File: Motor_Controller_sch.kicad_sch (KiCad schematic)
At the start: 59 parts, among them J1 1988804, J10 1988862, J11 Barrel_Jack_Switch, J12 +5V, J13 1988862, J14 1988817, J2 GND, J3 RX, J4 TX, J5 RESET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

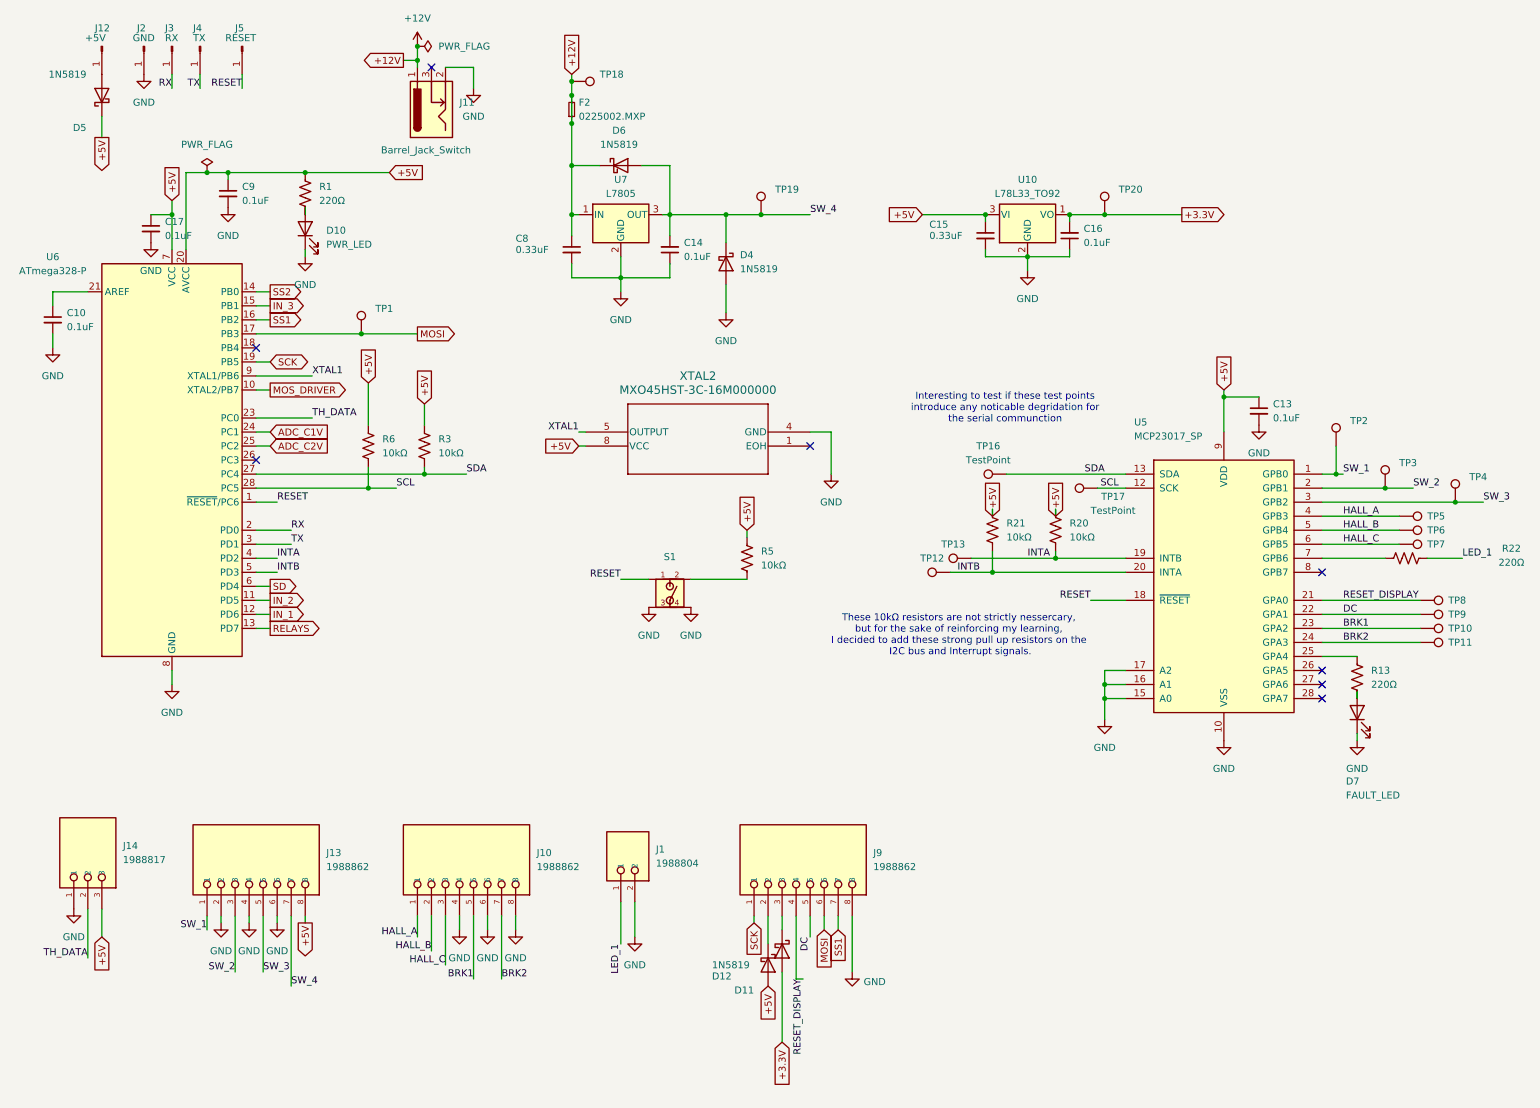
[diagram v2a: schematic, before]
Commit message: Reviewed gate resistors and removed MOSFET driver resistor
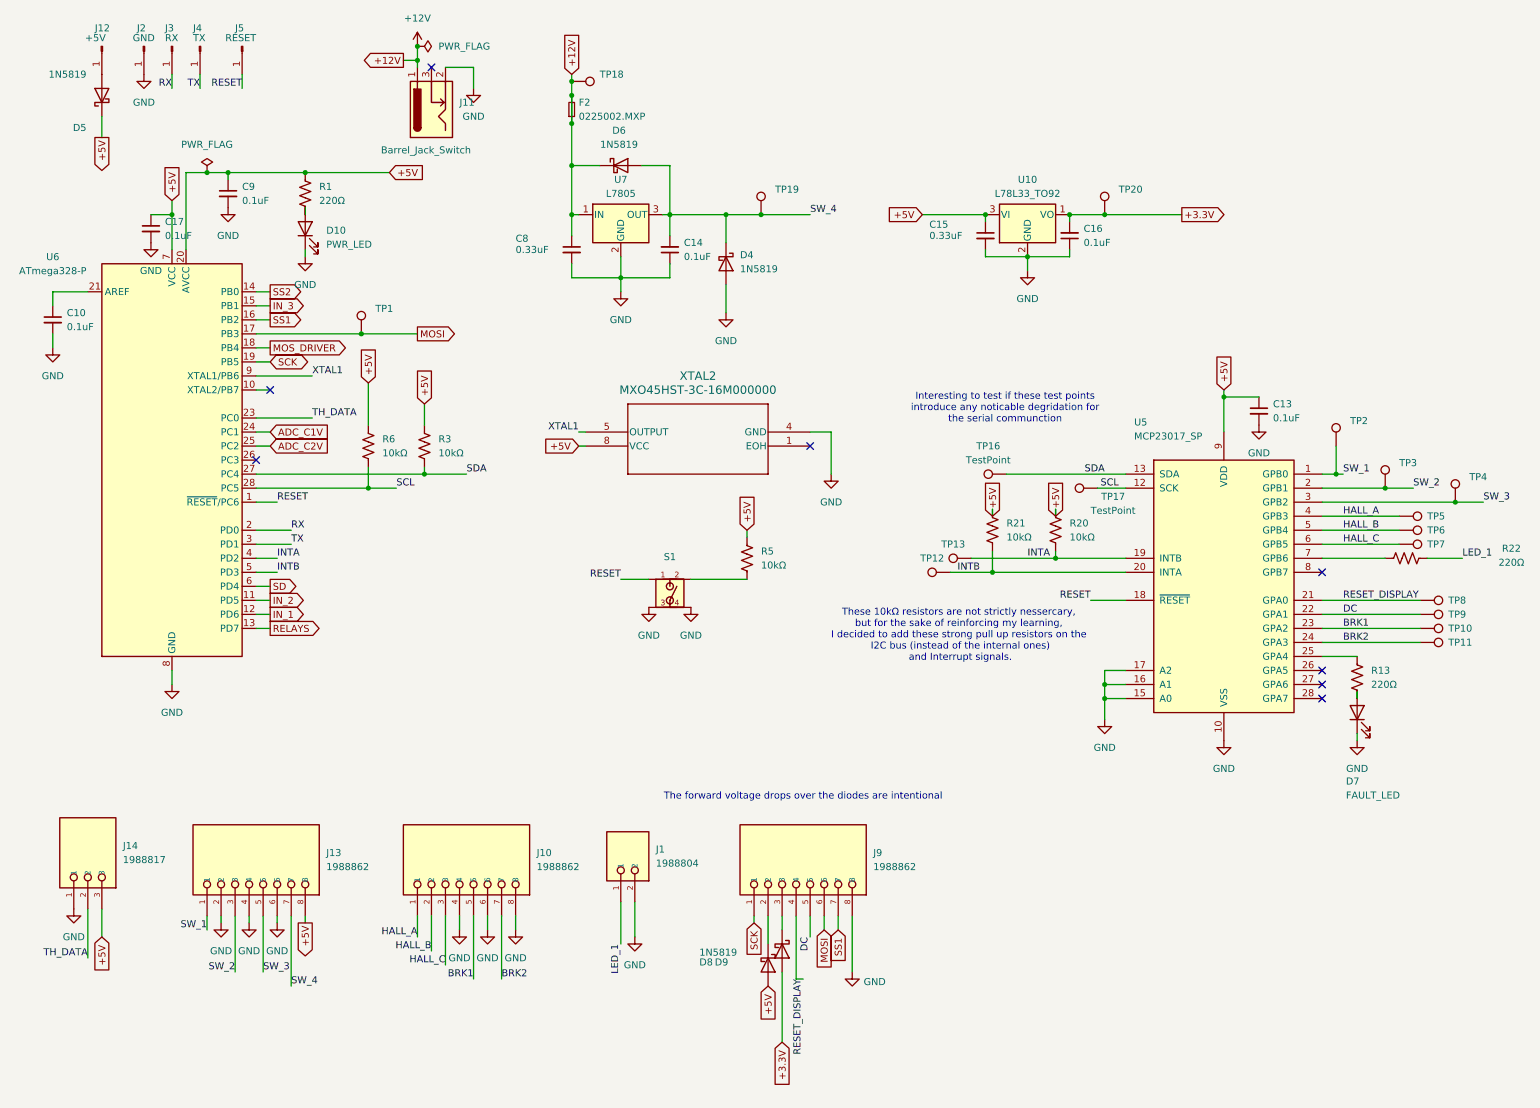
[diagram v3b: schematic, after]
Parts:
- removed D11, D12: 1N5819, Diode_THT:D_DO-41_SOD81_P10.16mm_Horizontal, symbol Diode:1N5819
- added D8, D9: 1N5819, Diode_THT:D_DO-41_SOD81_P10.16mm_Horizontal, symbol Diode:1N5819
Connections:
- net +3.3V: now also D9.2 (A)
- net +5V: now also D8.2 (A)
- net MOS_DRIVER: now also U6.18 (PB4); no longer U6.10 (XTAL2/PB7)
- net at J9.2: now also D8.1 (K)
- net at J9.3: now also D9.1 (K)
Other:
- note added: "The forward voltage drops over the diodes are intentional"
- note added: "These 10kΩ resistors are not strictly nessercary, but for the sake of reinforcing my learning, I decided to add these strong pull up resistors on the I2C bus (instead of the internal ones) and Interrupt signals."
- note removed: "These 10kΩ resistors are not strictly nessercary, but for the sake of reinforcing my learning, I decided to add these strong pull up resistors on the I2C bus and Interrupt signals."
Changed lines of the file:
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@@
 	)
 	(no_connect
-		(at 53.34 73.66)
+		(at 246.38 114.3)
 	)
 	(no_connect
-		(at 246.38 114.3)
+		(at 55.88 81.28)
 	)
 	(no_connect
@@
 	(wire
 		(pts
+			(xy 53.34 73.66) (xy 55.88 73.66)
+		)
+		(stroke
+			(width 0)
+			(type default)
+		)
+	)
+	(wire
+		(pts
 			(xy 153.67 176.53) (xy 153.67 180.34)
 		)
@@
 		)
 	)
-	(text "These 10kΩ resistors are not strictly nessercary, \nbut for the sake of reinforcing my learning, \nI decided to add these strong pull up resistors on the\n I2C bus and Interrupt signals."
+	(text "The forward voltage drops over the diodes are intentional"
+		(exclude_from_sim no)
+		(at 152.4 154.94 0)
+		(effects
+			(font
+				(size 1.27 1.27)
+			)
+		)
+	)
+	(text "These 10kΩ resistors are not strictly nessercary, \nbut for the sake of reinforcing my learning, \nI decided to add these strong pull up resistors on the\n I2C bus (instead of the internal ones)\n and Interrupt signals."
 		(exclude_from_sim no)
 		(at 180.594 125.73 0)
@@
 		)
 	)
+	(global_label "MOS_DRIVER"
+		(shape output)
+		(at 55.88 73.66 0)
+		(fields_autoplaced yes)
+		(effects
+			(font
+				(size 1.27 1.27)
+			)
+			(justify left)
+		)
+		(property "Intersheetrefs" "${INTERSHEET_REFS}"
+			(at 70.4766 73.66 0)
+			(effects
+				(font
+					(size 1.27 1.27)
+				)
+				(justify left)
+				(hide yes)
+			)
+		)
+	)
 	(global_label "+5V"
 		(shape input)
@@
 		)
 	)
-	(global_label "MOS_DRIVER"
-		(shape output)
-		(at 55.88 81.28 0)
-		(fields_autoplaced yes)
-		(effects
-			(font
-				(size 1.27 1.27)
-			)
-			(justify left)
-		)
-		(property "Intersheetrefs" "${INTERSHEET_REFS}"
-			(at 70.4766 81.28 0)
-			(effects
-				(font
-					(size 1.27 1.27)
-				)
-				(justify left)
-				(hide yes)
-			)
-		)
-	)
 	(global_label "ADC_C1V"
 		(shape input)
@@
 	)
 	(symbol
-		(lib_id "Diode:1N5819")
-		(at 146.05 185.42 270)
-		(unit 1)
-		(exclude_from_sim no)
-		(in_bom yes)
-		(on_board yes)
-		(dnp no)
-		(property "Reference" "D12"
-			(at 135.89 187.452 90)
-			(effects
-				(font
-					(size 1.27 1.27)
-				)
-				(justify left)
-			)
-		)
-		(property "Value" "1N5819"
-			(at 135.89 185.42 90)
-			(effects
-				(font
-					(size 1.27 1.27)
-				)
-				(justify left)
-			)
-		)
-		(property "Footprint" "Diode_THT:D_DO-41_SOD81_P10.16mm_Horizontal"
-			(at 141.605 185.42 0)
-			(effects
-				(font
-					(size 1.27 1.27)
-				)
-				(hide yes)
-			)
-		)
-		(property "Datasheet" "http://www.vishay.com/docs/88525/1n5817.pdf"
-			(at 146.05 185.42 0)
-			(effects
-				(font
-					(size 1.27 1.27)
-				)
-				(hide yes)
-			)
-		)
-		(property "Description" "40V 1A Schottky Barrier Rectifier Diode, DO-41"
-			(at 146.05 185.42 0)
-			(effects
-				(font
-					(size 1.27 1.27)
-				)
-				(hide yes)
-			)
-		)
-		(pin "2"
-		)
-		(pin "1"
-		)
-		(instances
-			(project "SuperCapacitorBike"
-				(path "/1096cbe7-ac56-48cb-aadd-3e4addcdbbb7/a964da0d-002d-40d7-a8b6-c48f0e32c7fd"
-					(reference "D12")
-					(unit 1)
-				)
-			)
-		)
-	)
-	(symbol
 		(lib_id "Connector:Conn_01x01_Pin")
 		(at 50.8 19.05 270)
@@
 	)
 	(symbol
+		(lib_id "Diode:1N5819")
+		(at 146.05 185.42 270)
+		(unit 1)
+		(exclude_from_sim no)
+		(in_bom yes)
+		(on_board yes)
+		(dnp no)
+		(property "Reference" "D8"
+			(at 133.604 184.912 90)
+			(effects
+				(font
+					(size 1.27 1.27)
+				)
+				(justify left)
+			)
+		)
+		(property "Value" "1N5819"
+			(at 133.604 184.912 90)
+			(effects
+				(font
+					(size 1.27 1.27)
+				)
+				(justify left)
+				(hide yes)
+			)
+		)
+		(property "Footprint" "Diode_THT:D_DO-41_SOD81_P10.16mm_Horizontal"
+			(at 141.605 185.42 0)
+			(effects
+				(font
+					(size 1.27 1.27)
+				)
+				(hide yes)
+			)
+		)
+		(property "Datasheet" "http://www.vishay.com/docs/88525/1n5817.pdf"
+			(at 146.05 185.42 0)
+			(effects
+				(font
+					(size 1.27 1.27)
+				)
+				(hide yes)
+			)
+		)
+		(property "Description" "40V 1A Schottky Barrier Rectifier Diode, DO-41"
+			(at 146.05 185.42 0)
+			(effects
+				(font
+					(size 1.27 1.27)
+				)
+				(hide yes)
+			)
+		)
+		(pin "2"
+		)
+		(pin "1"
+		)
+		(instances
+			(project "SuperCapacitorBike"
+				(path "/1096cbe7-ac56-48cb-aadd-3e4addcdbbb7/a964da0d-002d-40d7-a8b6-c48f0e32c7fd"
+					(reference "D8")
+					(unit 1)
+				)
+			)
+		)
+	)
+	(symbol
 		(lib_id "Connector:TestPoint")
 		(at 260.35 109.22 270)
@@
 	)
 	(symbol
+		(lib_id "Diode:1N5819")
+		(at 148.59 182.88 270)
+		(unit 1)
+		(exclude_from_sim no)
+		(in_bom yes)
+		(on_board yes)
+		(dnp no)
+		(property "Reference" "D9"
+			(at 136.398 184.912 90)
+			(effects
+				(font
+					(size 1.27 1.27)
+				)
+				(justify left)
+			)
+		)
+		(property "Value" "1N5819"
+			(at 133.604 183.134 90)
+			(effects
+				(font
+					(size 1.27 1.27)
+				)
+				(justify left)
+			)
+		)
+		(property "Footprint" "Diode_THT:D_DO-41_SOD81_P10.16mm_Horizontal"
+			(at 144.145 182.88 0)
+			(effects
+				(font
+					(size 1.27 1.27)
+				)
+				(hide yes)
+			)
+		)
+		(property "Datasheet" "http://www.vishay.com/docs/88525/1n5817.pdf"
+			(at 148.59 182.88 0)
+			(effects
+				(font
+					(size 1.27 1.27)
+				)
+				(hide yes)
+			)
+		)
+		(property "Description" "40V 1A Schottky Barrier Rectifier Diode, DO-41"
+			(at 148.59 182.88 0)
+			(effects
+				(font
+					(size 1.27 1.27)
+				)
+				(hide yes)
+			)
+		)
+		(pin "2"
+		)
+		(pin "1"
+		)
+		(instances
+			(project "SuperCapacitorBike"
+				(path "/1096cbe7-ac56-48cb-aadd-3e4addcdbbb7/a964da0d-002d-40d7-a8b6-c48f0e32c7fd"
+					(reference "D9")
+					(unit 1)
+				)
+			)
+		)
+	)
+	(symbol
 		(lib_id "power:GND")
 		(at 57.15 177.8 0)
@@
 					(unit 1)
 				)
-			)
-		)
-	)
-	(symbol
-		(lib_id "Diode:1N5819")
-		(at 148.59 182.88 270)
-		(unit 1)
-		(exclude_from_sim no)
-		(in_bom yes)
-		(on_board yes)
-		(dnp no)
-		(property "Reference" "D11"
-			(at 139.954 189.992 90)
-			(effects
-				(font
-					(size 1.27 1.27)
-				)
-				(justify left)
-			)
-		)
-		(property "Value" "1N5819"
-			(at 150.876 192.278 90)
-			(effects
-				(font
-					(size 1.27 1.27)
-				)
-				(justify left)
-				(hide yes)
-			)
-		)
-		(property "Footprint" "Diode_THT:D_DO-41_SOD81_P10.16mm_Horizontal"
-			(at 144.145 182.88 0)
-			(effects
-				(font
-					(size 1.27 1.27)
-				)
-				(hide yes)
-			)
-		)
-		(property "Datasheet" "http://www.vishay.com/docs/88525/1n5817.pdf"
-			(at 148.59 182.88 0)
-			(effects
-				(font
-					(size 1.27 1.27)
-				)
-				(hide yes)
-			)
-		)
-		(property "Description" "40V 1A Schottky Barrier Rectifier Diode, DO-41"
-			(at 148.59 182.88 0)
-			(effects
-				(font
-					(size 1.27 1.27)
-				)
-				(hide yes)
-			)
-		)
-		(pin "2"
-		)
-		(pin "1"
-		)
-		(instances
-			(project "SuperCapacitorBike"
-				(path "/1096cbe7-ac56-48cb-aadd-3e4addcdbbb7/a964da0d-002d-40d7-a8b6-c48f0e32c7fd"
-					(reference "D11")
-					(unit 1)
-				)
